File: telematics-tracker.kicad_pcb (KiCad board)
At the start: 4 copper layers, 82 x 62 mm, 216 parts, among them J1 WAFER-MX3.0-12PZZ, J2 B3B-XH-A, Q1 AM2390N-TP, Q10 MMBT3904, Q11 MMBT3904, Q12 MMBT3904, Q13 MMBT3906, Q14 MMBT3904, Q2 AM2390N-TP, Q3 AO3401A, Q4 MMBT3904, Q5 MMBT3904, Q6 MMBT3904, Q7 MMBT3904, Q8 MMBT3904, Q9 MMBT3904, U1 EC200UCNAA-N05-SGNSA, U2 AT32F403ACGT7, U3 QMI8658B, U4 SIT1051AT/3, U5 EG11752, U6 BQ25606RGER, U7 GD25Q64ESIGR, U8 TXB0104PWR, U9 ME6211C33M5G, X1 NANO-SIM, X2 MFF2-eSIM-pads, Y1 8MHz, Y2 32.768kHz

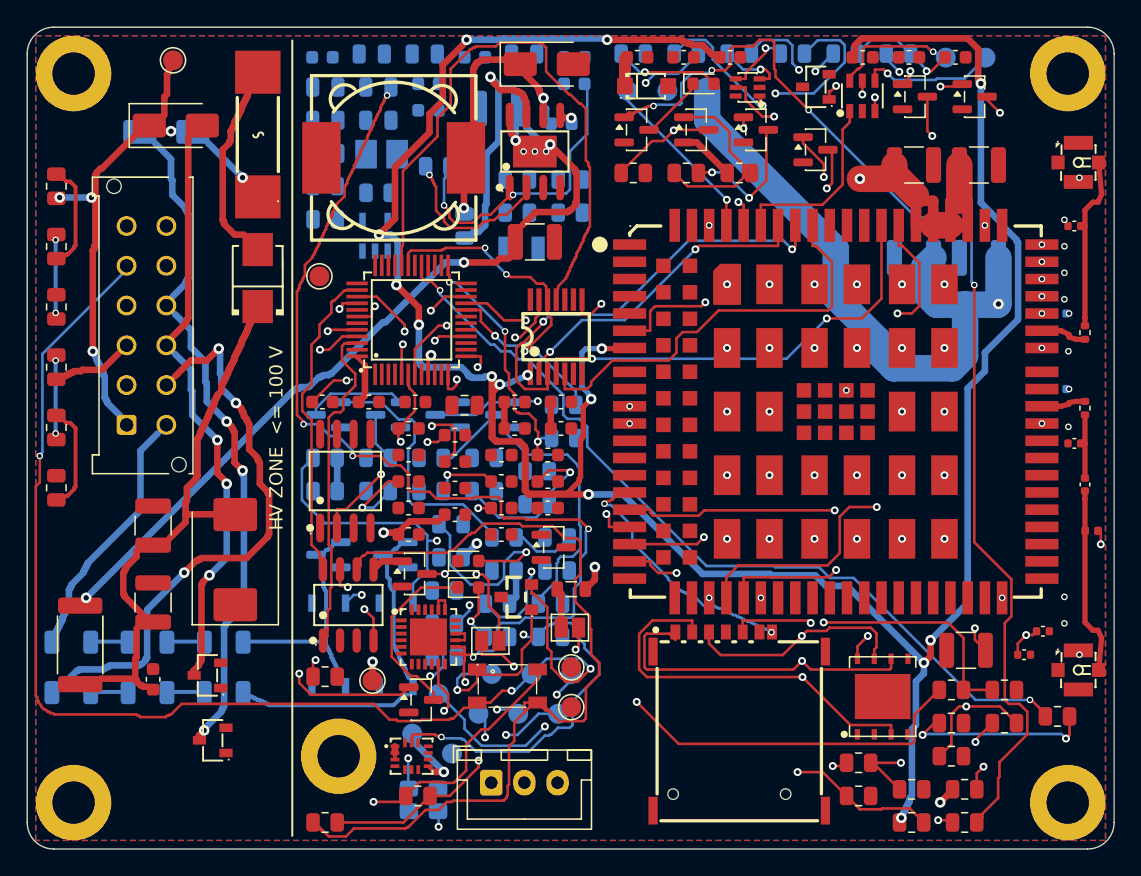
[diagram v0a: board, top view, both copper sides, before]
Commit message: Cluster repair v2: tile around the DI optos, H5, and the buck B-field
v1 dropped C62/C63 onto the optos' anchors and its displacement chain
pushed Y1 (the 8 MHz crystal) under the buck. Y1+C1/C2 now sit at the MCU,
the U6 ring right of the optos, the displaced caps and debug TPs re-homed.

Co-Authored-By: Claude Opus 5 (1M context) <noreply@anthropic.com>
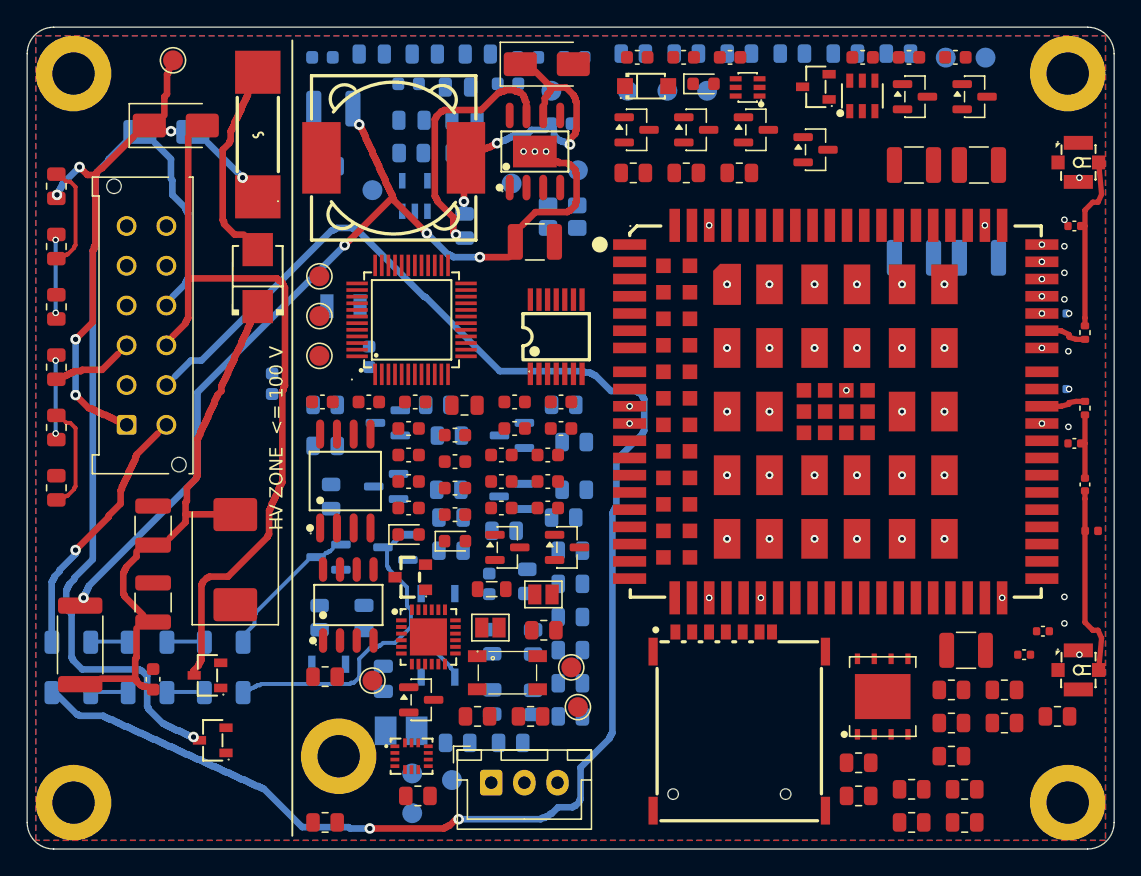
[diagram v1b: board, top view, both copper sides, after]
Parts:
- C3, C4: moved to B.Cu
- R2, R21, R22, TP28, TP3: moved to F.Cu
- moved TP7 50.6 mm to (39.5, 4.80)
- moved C62 47.1 mm to (26.9, 49.2), turned to 90 degrees
- moved Y1 45.2 mm to (40.4, 14.3)
- moved L3 43.5 mm to (28.2, 53.1)
- moved C63 42.8 mm to (25.4, 44.6), turned to 90 degrees
- moved TP4 41.2 mm to (41.5, 10.8)
- moved TP6 41.1 mm to (26.0, 12.3)
- moved TP5 40.2 mm to (36.5, 11.8)
- moved C64 39.7 mm to (34.9, 42.0), turned to 90 degrees
- moved R89 38.5 mm to (35.1, 50.9), turned to 90 degrees
- moved R87 37.0 mm to (38.2, 50.9), turned to 90 degrees
- moved R86 35.8 mm to (38.2, 46.4), turned to 90 degrees
- moved R85 33.5 mm to (37.7, 41.8), turned to 90 degrees
- moved R88 32.9 mm to (35.1, 46.4), turned to 90 degrees
- moved TP28 29.9 mm to (22.0, 21.8), turned to 0 degrees
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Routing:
- net /modem_rf/VDD_EXT_1V8: track 206.5 -> 0.00 mm, vias 15 -> 0
- net MODEM_STATUS: track 132.9 -> 0.00 mm, vias 3 -> 0
- net /io/CANL: track 91.2 -> 0.00 mm, vias 3 -> 0
- net /modem_rf/Q12_B: track 86.3 -> 0.00 mm, vias 4 -> 0
- net /power/VBAT_BT: track 84.7 -> 0.00 mm, vias 6 -> 0
- net /modem_rf/SIM_DATA: track 84.3 -> 0.00 mm, vias 2 -> 0
- net /io/DI2_IN: track 42.7 -> 122.1 mm, vias 3 -> 2
- net /modem_rf/SIM_CLK: track 78.0 -> 0.00 mm, vias 2 -> 0
- net MODEM_RESET: track 74.5 -> 0.00 mm, vias 2 -> 0
- net /modem_rf/USIM_VDD: track 72.5 -> 0.00 mm, vias 3 -> 0
- net /modem_rf/VBAT_MODEM: track 71.2 -> 0.00 mm, vias 2 -> 0
- net /modem_rf/SIM_RST: track 67.3 -> 0.00 mm, vias 2 -> 0
- net MODEM_PWR_EN: track 64.5 -> 0.00 mm, vias 2 -> 0
- net /io/CANL_T: track 64.4 -> 0.00 mm
- net /modem_rf/Q9_B: track 63.7 -> 0.00 mm, vias 3 -> 0
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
